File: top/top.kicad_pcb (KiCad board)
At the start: 2 copper layers, 28.8 x 40.6 mm, 25 parts, among them P1 CONN_10, P2 CONN_5, U1 IQS572, U4 ESD

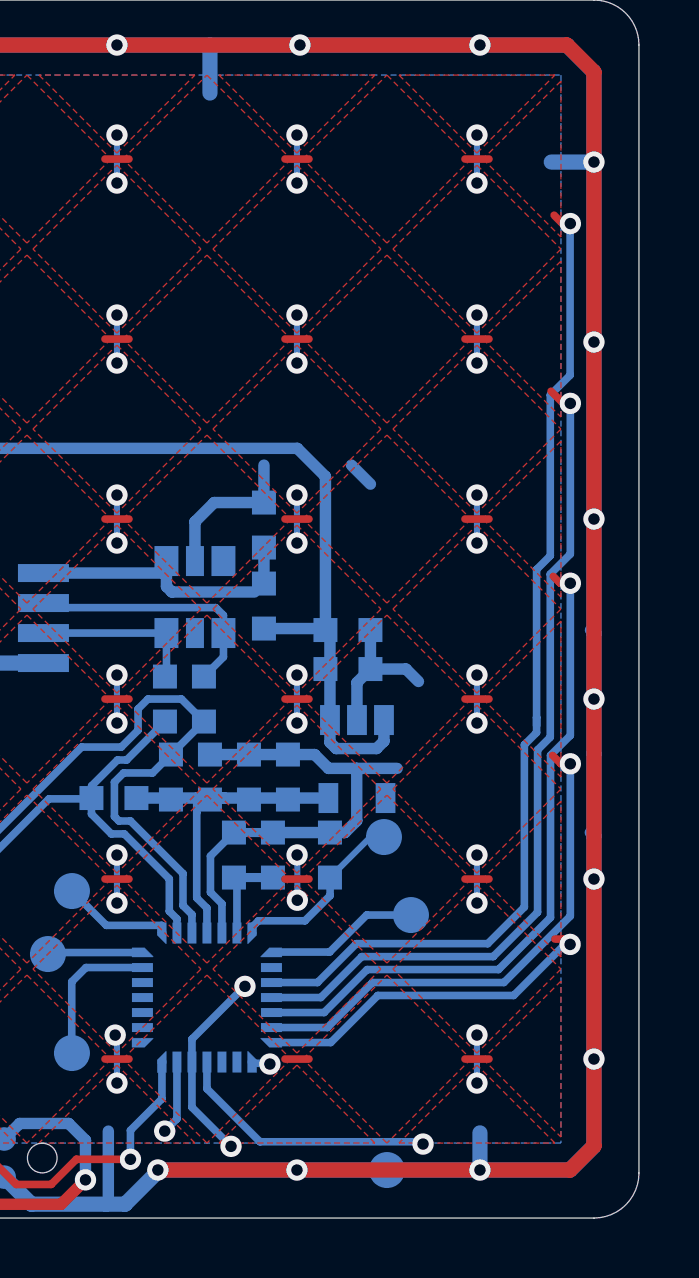
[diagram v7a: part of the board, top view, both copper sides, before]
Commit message: Connect unconnected wires and remove the diamond pattern from the bottom left corner.
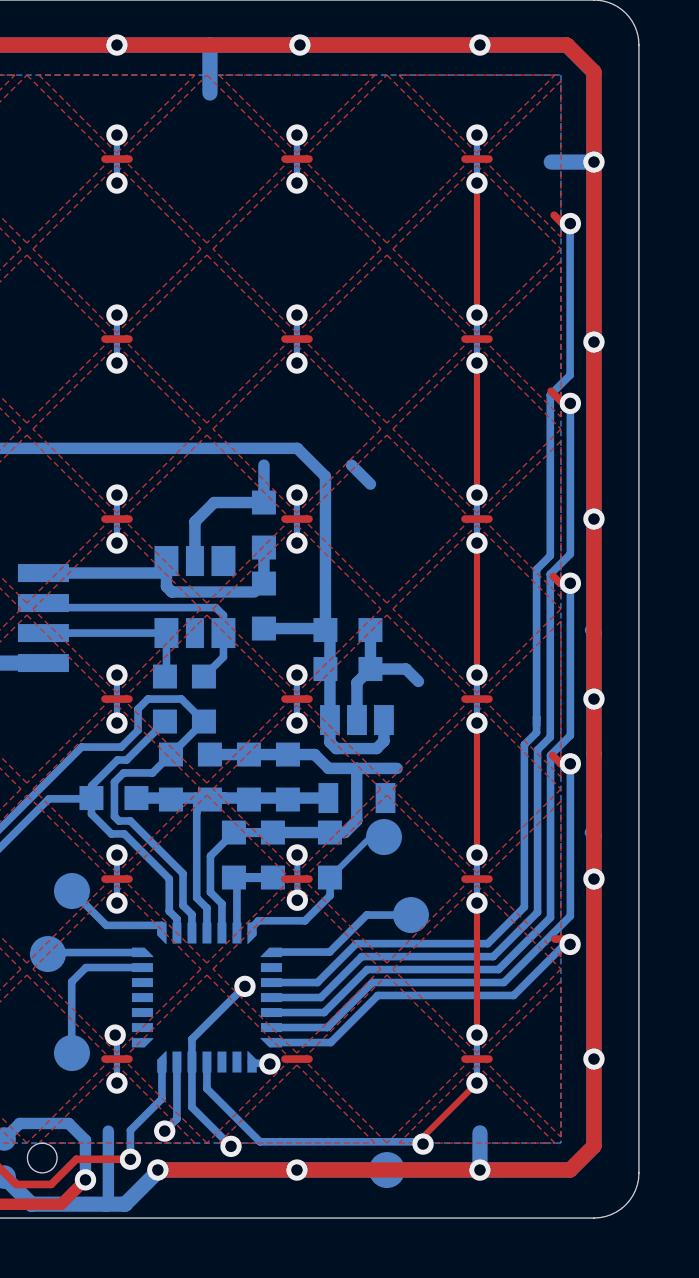
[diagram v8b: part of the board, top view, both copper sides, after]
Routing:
- net /TX0: track 18.5 -> 43.2 mm
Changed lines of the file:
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@@
-(kicad_pcb (version 20171130) (host pcbnew "(5.0.0)")
+(kicad_pcb (version 20171130) (host pcbnew 5.1.2-f72e74a~84~ubuntu18.04.1)
   (general
     (thickness 1.6)
-    (drawings 63)
-    (tracks 400)
+    (drawings 59)
+    (tracks 407)
     (zones 0)
     (modules 25)
@@
   )
   (setup
-    (last_trace_width 0.508)
+    (last_trace_width 0.2032)
     (user_trace_width 0.2032)
     (user_trace_width 0.254)
@@
     (zone_45_only yes)
     (trace_min 0.2032)
-    (segment_width 0.3)
-    (edge_width 0.1)
     (via_size 0.7112)
     (via_drill 0.381)
@@
     (uvia_min_size 0.508)
     (uvia_min_drill 0.127)
+    (edge_width 0.1)
+    (segment_width 0.3)
     (pcb_text_width 0.3)
     (pcb_text_size 1.5 1.5)
@@
     (pad_to_mask_clearance 0)
     (aux_axis_origin 0 0)
-    (visible_elements 7FFFFF6F)
+    (visible_elements 7FFFEF6F)
     (pcbplotparams
       (layerselection 0x00030_ffffffff)
@@
     (uvia_dia 0.7112)
     (uvia_drill 0.381)
+    (diff_pair_width 0.254)
     (diff_pair_gap 0.254)
-    (diff_pair_width 0.254)
     (add_net +3V3)
     (add_net +5V)
@@
   (gr_arc (start 218.600003 157.100012) (end 218.6 158.6) (angle -89.99900791) (layer Edge.Cuts) (width 0.01))
   (gr_line (start 220.1 157.1) (end 220.1 119.5) (angle 90) (layer Edge.Cuts) (width 0.01))
-  (gr_line (start 186.2 154.1) (end 183.4 151.3) (layer Eco1.User) (width 0.2))
-  (gr_line (start 189 151.3) (end 186.2 154.1) (layer Eco1.User) (width 0.2))
-  (gr_line (start 186.2 148.5) (end 189 151.3) (layer Eco1.User) (width 0.2))
-  (gr_line (start 183.4 151.3) (end 186.2 148.5) (layer Eco1.User) (width 0.2))
   (gr_text "PCB_ID: touchpad_top_1.0.0" (at 206.1 118.7) (layer B.SilkS)
     (effects (font (size 0.75 0.75) (thickness 0.15)) (justify mirror))
@@
   (segment (start 201.8538 144.6276) (end 201.8538 144.1958) (width 0.254) (layer B.Cu) (net 11))
   (segment (start 201.8538 144.1958) (end 202.7174 143.3322) (width 0.254) (layer B.Cu) (net 11))
-  (segment (start 195.13 157.235) (end 195.13 157.360198) (width 0.254) (layer B.Cu) (net 39))
   (segment (start 205.85 144.6) (end 205.8 144.65) (width 0.381) (layer B.Cu) (net 12))
   (segment (start 205.7 148.2706) (end 205.359022 147.929622) (width 0.254) (layer B.Cu) (net 12))
@@
   (segment (start 205.7 153.4) (end 205.7 154.2904) (width 0.254) (layer B.Cu) (net 22))
   (segment (start 205.7 154.2904) (end 207.4672 156.0576) (width 0.254) (layer B.Cu) (net 22))
+  (segment (start 214.7 124.1) (end 214.7 128.5) (width 0.2032) (layer F.Cu) (net 22))
+  (segment (start 214.7 130.1) (end 214.7 134.5) (width 0.2032) (layer F.Cu) (net 22))
+  (segment (start 214.7 136.1) (end 214.7 140.5) (width 0.2032) (layer F.Cu) (net 22))
+  (segment (start 214.7 142.1) (end 214.7 146.5) (width 0.2032) (layer F.Cu) (net 22))
+  (segment (start 214.7 148.1) (end 214.7 152.5) (width 0.2032) (layer F.Cu) (net 22))
+  (segment (start 212.902798 155.897202) (end 212.902798 156.1338) (width 0.2032) (layer F.Cu) (net 22))
+  (segment (start 214.7 154.1) (end 212.902798 155.897202) (width 0.2032) (layer F.Cu) (net 22))
   (via (at 208.7 122.5) (size 0.7112) (drill 0.381) (layers F.Cu B.Cu) (net 23))
   (via (at 208.7 124.1) (size 0.7112) (drill 0.381) (layers F.Cu B.Cu) (net 23))
@@
   (segment (start 201.168 153.0858) (end 201.1934 153.0604) (width 0.254) (layer B.Cu) (net 33))
   (segment (start 201.1934 153.0604) (end 201.1934 150.7236) (width 0.254) (layer B.Cu) (net 33))
+  (segment (start 195.13 157.235) (end 195.13 157.360198) (width 0.254) (layer B.Cu) (net 39))
   (zone (net 16) (net_name /RX0) (layer F.Cu) (hatch edge 0.508)
     (connect_pads (clearance 0.254))
